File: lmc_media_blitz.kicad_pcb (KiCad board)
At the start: 2 copper layers, 76.2 x 114.3 mm, 83 parts, among them J3 Conn_ARM_JTAG_SWD_10, Q1 2N7002, Q2 2N7002, U1 TPS61222DCK, U10 SK9822, U11 SK9822, U12 SK9822, U13 SK9822, U14 SK9822, U2 XC6206PxxxMR, U4 ST25R3911B-AQFT, U5 LPC804M101JHI33, Y1 27.12MHz

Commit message: Updated MCU and connector pinout to make routing more convenient.  Power circuit still to be routed
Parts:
- added D1: SSL54B, Diode_SMD:D_SMB, F.Cu at (165.8, -34.2)
- added J4: Conn_01x12, Connector_PinSocket_2.54mm:PinSocket_1x12_P2.54mm_Vertical, F.Cu at (271.5, 88.6)
- added NT1: NetTie_2, NetTie:NetTie-2_SMD_Pad0.5mm, F.Cu at (163.9, -43.6)
- added R10: 10K, Resistor_SMD:R_0805_2012Metric, F.Cu at (259.9, 84.1)
- added R11: 10K, Resistor_SMD:R_0805_2012Metric, F.Cu at (269.5, 84.1)
- added R9: 10K, Resistor_SMD:R_0805_2012Metric, F.Cu at (250.3, 84.1)
- added SW1: SW_Push, Button_Switch_SMD:SW_Push_1P1T_XKB_TS-1187A, F.Cu at (246.6, 80.0)
- added SW2: SW_Push, Button_Switch_SMD:SW_Push_1P1T_XKB_TS-1187A, F.Cu at (256.3, 80.0)
- added SW3: SW_Push, Button_Switch_SMD:SW_Push_1P1T_XKB_TS-1187A, F.Cu at (266.0, 80.0)
- added TP10: TestPoint_Small, TestPoint:TestPoint_Pad_D1.5mm, F.Cu at (265.4, 86.9)
- added TP8: TestPoint_Small, TestPoint:TestPoint_Pad_D1.5mm, F.Cu at (253.7, 86.9)
- added TP9: TestPoint_Small, TestPoint:TestPoint_Pad_D1.5mm, F.Cu at (260.4, 86.9)
- added U3: STM32F030C8Tx, Package_QFP:LQFP-48_7x7mm_P0.5mm, F.Cu at (258.6, 103.6)
- added U6: SK9822, footprints:OPSCO_SK9822, F.Cu at (257.9, 126.2)
- added U7: SK9822, footprints:OPSCO_SK9822, F.Cu at (266.6, 126.2)
- added U8: SK9822, footprints:OPSCO_SK9822, F.Cu at (275.2, 126.2)
- C10, C14, C9: value 10nF -> 100nF
- C11: value 1uF -> 10nF
- C12, C16, C18, C6: value 10nF -> 1uF; footprint Capacitor_SMD:C_0603_1608Metric -> Capacitor_SMD:C_0805_2012Metric
- C13, C15: value 2.2uF -> 100nF
- C17: value 2.2uF -> 1uF; footprint Capacitor_SMD:C_0603_1608Metric -> Capacitor_SMD:C_0805_2012Metric
- C19: footprint Capacitor_SMD:C_0603_1608Metric -> Capacitor_SMD:C_0805_2012Metric
- C2: value 10uF -> 22uF
- C20: value 150pF -> 1uF
- C5: value 0.1uF -> 1uF; footprint Capacitor_SMD:C_0603_1608Metric -> Capacitor_SMD:C_0805_2012Metric
- C8: value 1uF -> 100nF
- J3: value Conn_ARM_JTAG_SWD_10 -> Conn_01x12; footprint Connector_PinHeader_1.27mm:PinHeader_2x05_P1.27mm_Vertical_SMD -> Connector_PinSocket_2.54mm:PinSocket_1x12_P2.54mm_Vertical
- L1: value 4.7uH -> 4u7; footprint Inductor_SMD:L_Taiyo-Yuden_MD-3030 -> Inductor_SMD:L_Changjiang_FNR4030S
- Q1, Q2: value 2N7002 -> BSS138W; footprint Package_TO_SOT_SMD:SOT-23 -> Package_TO_SOT_SMD:SOT-23W
- R1, R2: value 10K -> 4k7
- R7, R8: value 1R -> 10K
- TP4, TP5, TP6, TP7: footprint TestPoint:TestPoint_Pad_D2.0mm -> TestPoint:TestPoint_Pad_D1.5mm
- U1: value TPS61222DCK -> XC6206PxxxMR; footprint Package_TO_SOT_SMD:Texas_R-PDSO-G6 -> Package_TO_SOT_SMD:SOT-23-3
- U2: value XC6206PxxxMR -> TPS613222ADBV; footprint Package_TO_SOT_SMD:SOT-23-3 -> Package_TO_SOT_SMD:SOT-23-5
- U4: value ST25R3911B-AQFT -> SK9822; footprint Package_DFN_QFN:QFN-32-1EP_5x5mm_P0.5mm_EP3.6x3.6mm -> footprints:OPSCO_SK9822
- U5: value LPC804M101JHI33 -> SK9822; footprint Package_DFN_QFN:QFN-32-1EP_5x5mm_P0.5mm_EP3.7x3.7mm -> footprints:OPSCO_SK9822
- moved C15 132.4 mm to (270.6, 80.0), turned to 90 degrees
- moved C20 124.5 mm to (275.2, 130.3), turned to 180 degrees
- moved C1 123.4 mm to (164.9, -42.6), turned to 180 degrees
- moved C14 123.2 mm to (260.9, 80.0), turned to 90 degrees
- moved C2 123.0 mm to (168.7, -42.6), turned to 0 degrees
- moved U1 121.0 mm to (153.4, -44.1)
- moved R2 120.5 mm to (259.2, 93.7), turned to 180 degrees
- moved C3 119.1 mm to (150.6, -44.5)
- moved C4 119.0 mm to (156.2, -44.5), turned to 90 degrees
- moved R1 117.6 mm to (259.2, 91.7), turned to 180 degrees
- moved TP1 117.4 mm to (156.2, -38.3)
- moved TP2 117.4 mm to (188.8, -29.2)
- moved C10 116.6 mm to (261.9, 109.7), turned to 180 degrees
- moved U2 115.7 mm to (167.5, -39.1), turned to 90 degrees
- moved L1 115.3 mm to (163.1, -39.0), turned to -90 degrees
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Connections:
- C1 pad 2: +BATT -> /ADC_IN0
- C10 pad 1: +5V -> +3V3
- C11 pad 1: +5V -> +3V3
- C12 pad 1: /NFC/VSP_RF -> +3V3
- C13 pad 1: GND -> /SW1
- C13 pad 2: /NFC/VSP_RF -> GND
- C14 pad 1: /NFC/VSP_A -> /SW2
- C15 pad 1: GND -> /SW3
- C15 pad 2: /NFC/VSP_A -> GND
- C16 pad 1: /NFC/VSP_D -> +5V
- C17 pad 1: GND -> +5V
- C17 pad 2: /NFC/VSP_D -> GND
- C18 pad 1: /NFC/A_REF -> +5V
- C19 pad 1: /NFC/A_REF -> +5V
- C20 pad 1: GND -> +5V
- C20 pad 2: /NFC/RFI1 -> GND
- C6 pad 1: +3V3 -> +5V
- J3 pad 1: +3V3 -> +5V
- J3 pad 10: /nRESET -> GND
- J3 pad 2: /SWDIO -> GND
- J3 pad 3: GND -> +3V3
- J3 pad 4: /SWCLK -> +3V3
- J3 pad 6: unconnected-(J3-SWO/TDO-Pad6) -> /I2C1_SCL
- J3 pad 7: unconnected-(J3-KEY-Pad7) -> /I2C1_SDA
- J3 pad 8: unconnected-(J3-NC/TDI-Pad8) -> GND
- J3 pad 9: GND -> /BOOT0
- L1 pad 1: +BATT -> /ADC_IN0
- L1 pad 2: /L -> /BOOST_SW
- Q1 pad 1: /SPI0_MOSI -> /SPI1_SCK
- Q1 pad 2: /SPI0_MOSI -> /SPI1_SCK
- Q1 pad 3: /LEDs/SDI -> /LEDs/CKI
- Q2 pad 1: /SPI0_SCKB -> /SPI1_MOSI
- Q2 pad 2: /SPI0_SCKB -> /SPI1_MOSI
- Q2 pad 3: /LEDs/CKI -> /LEDs/SDI
- R1 pad 1: GND -> +3V3
- R1 pad 2: /SWCLK -> /I2C1_SDA
- R2 pad 2: /SWDIO -> /I2C1_SCL
- R3 pad 2: /SPI0_MOSI -> /nRST
- R4 pad 1: +5V -> +3V3
- R4 pad 2: /LEDs/SDI -> /SPI1_SCK
- R5 pad 1: +3V3 -> +5V
- R5 pad 2: /SPI0_SCKB -> /LEDs/CKI
- R6 pad 1: +5V -> +3V3
- R6 pad 2: /LEDs/CKI -> /SPI1_MOSI
- R7 pad 1: /NFC/ANT_MATCH1 -> +5V
- R7 pad 2: /NFC/ANT_DAMP1 -> /LEDs/SDI
- R8 pad 1: /NFC/ANT_MATCH2 -> /BOOT0
- R8 pad 2: /NFC/ANT_DAMP2 -> GND
- TP1 pad 1: GND -> +5V
- TP2 pad 1: /CAPT_X1 -> +3V3
- TP3 pad 1: +5V -> GND
- TP4 pad 1: +3V3 -> /ADC_IN0
- TP5 pad 1: +BATT -> /LEDs/CKI
- TP6 pad 1: /CAPT_X0 -> /SPI1_MISO
- TP7 pad 1: /CAPT_X2 -> /LEDs/SDI
- U1 pad 1: +BATT -> GND
- U1 pad 2: +5V -> +3V3
- U1 pad 3: GND -> +5V
- U2 pad 1: GND -> /BOOST_SW
- U2 pad 2: +3V3 -> GND
- U2 pad 3: +5V -> unconnected-(U2-NC-Pad3)
- U4 pad 1: +3V3 -> /LEDs/SDI
- U4 pad 2: unconnected-(U4-CSO-Pad2) -> /LEDs/CKI
- U4 pad 3: /NFC/VSP_D -> GND
- U4 pad 4: /NFC/XTO -> +5V
- U4 pad 5: /NFC/XTI -> /LEDs/LED2_CKI
- U4 pad 6: GND -> /LEDs/LED2_SDI
- U5 pad 1: /SPI0_SCKB -> /LEDs/LED2_SDI
- U5 pad 2: +BATT -> /LEDs/LED2_CKI
- U5 pad 3: unconnected-(U5-PIO0_12-Pad3) -> GND
- U5 pad 4: /nRESET -> +5V
- U5 pad 5: unconnected-(U5-PIO0_4/ADC_11/TRSTN-Pad5) -> /LEDs/LED3_CKI
- U5 pad 6: /SWCLK -> /LEDs/LED3_SDI
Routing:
- net (no net): track 0.00 -> 97.5 mm, vias 0 -> 2
- net GND: track 1.81 -> 74.3 mm, vias 169 -> 185
- net /nRST: track 0.00 -> 70.7 mm, vias 0 -> 4
- net +5V: track 225.4 -> 291.9 mm, vias 5 -> 6
- net /SPI0_MOSI: track 45.4 -> 0.00 mm, vias 4 -> 0
- net /SW1: track 0.00 -> 37.4 mm
- net +3V3: track 131.5 -> 167.4 mm, vias 3 -> 11
- net /SW3: track 0.00 -> 33.9 mm
- net /I2C1_SDA: track 0.00 -> 33.4 mm
- net /SW2: track 0.00 -> 29.5 mm
- net /I2C1_SCL: track 0.00 -> 27.6 mm
- net /SPI0_SCKB: track 25.1 -> 0.00 mm
- net /NFC_IRQ: track 19.8 -> 0.00 mm, vias 2 -> 0
- net /SPI2_NSS: track 0.00 -> 17.6 mm
- net /SPI2_SCK: track 0.00 -> 15.5 mm
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- added copper zone on F.Cu, net /BOOST_SW
- removed copper zone on F.Cu, net /L
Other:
- board text added: "NRST"
- board text added: "PA10/ RX"
- board text added: "PA9/TX"
- board text added: "PB12/CS"
- board text added: "PB13/SCK"
- board text added: "PB14/ MISO"
- board text added: "PB15/ MOSI"
- board text added: "SWCLK"
- board text added: "SWDIO"

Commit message: Changed board shape to be narrow around the pin headers to fit on a breadboard.  Still not sufficiently narrow
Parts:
- removed AE1: Antenna_Loop, footprints:badge_antenna
- removed C21, C36: 12pF, Capacitor_SMD:C_0805_2012Metric
- removed C22, C35: 100pF, Capacitor_SMD:C_0805_2012Metric
- removed C23, C24: 15pF, Capacitor_SMD:C_0603_1608Metric
- removed C25, C33: 470pF, Capacitor_SMD:C_0805_2012Metric
- removed C26, C34: 220pF, Capacitor_SMD:C_0805_2012Metric
- removed C27, C28, C29, C30, C31: 1uF, Capacitor_SMD:C_0805_2012Metric
- removed C32: 22nF, Capacitor_SMD:C_0805_2012Metric
- removed C37: 150pF, Capacitor_SMD:C_0805_2012Metric
- removed C38: 10uF, Capacitor_SMD:C_0805_2012Metric
- removed C39: 0.1uF, Capacitor_SMD:C_0603_1608Metric
- removed C40: 10nF, Capacitor_SMD:C_0603_1608Metric
- removed L2, L3: 270nH, Inductor_SMD:L_0805_2012Metric
- removed S1, S2, S3: ~, footprints:CapTouchButton
- removed U10, U11, U12, U13, U14: SK9822, footprints:OPSCO_SK9822
- removed Y1: 27.12MHz, Crystal:Crystal_SMD_Abracon_ABM8G-4Pin_3.2x2.5mm
- added TP11: TestPoint_Small, TestPoint:TestPoint_Pad_D1.5mm, F.Cu at (253.7, 86.9)
- TP1, TP2, TP3: footprint TestPoint:TestPoint_Pad_D2.0mm -> TestPoint:TestPoint_Pad_D1.5mm
- moved NT1 107.4 mm to (138.7, 60.7), turned to 90 degrees
- moved C1 101.9 mm to (138.7, 55.8), turned to -90 degrees
- moved C2 98.6 mm to (138.7, 51.3), turned to 90 degrees
- moved C3 98.2 mm to (154.2, 53.7)
- moved C4 98.2 mm to (159.8, 53.7)
- moved U1 98.2 mm to (157.0, 54.0)
- moved L1 97.2 mm to (142.2, 55.9), turned to 0 degrees
- moved U2 94.2 mm to (142.0, 51.6), turned to 180 degrees
- moved TP2 91.3 mm to (159.8, 57.4)
- moved TP1 90.0 mm to (151.6, 51.6)
- moved D1 89.6 mm to (147.3, 53.5), turned to -90 degrees
- moved TP8 35.6 mm to (252.5, 122.4)
- moved Q2 33.7 mm to (257.0, 118.4)
- moved R6 33.7 mm to (257.0, 115.3)
- moved R7 33.7 mm to (257.0, 121.4)
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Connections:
- C5 pad 1: +3V3 -> +5V
- C6 pad 1: +5V -> +3V3
- J3 pad 1: +5V -> GND
- J3 pad 11: /PB2 -> /GPIO_EXTI2
- J3 pad 12: /GPIO_EXTI10 -> /PA1
- J3 pad 2: GND -> +3V3
- J3 pad 4: +3V3 -> +5V
- TP10 pad 1: /SW3 -> /SW2
- TP5 pad 1: /LEDs/CKI -> /SPI1_NSS
- TP6 pad 1: /SPI1_MISO -> /LEDs/CKI
- TP7 pad 1: /LEDs/SDI -> /SPI1_MISO
- TP8 pad 1: /SW1 -> /LEDs/SDI
- TP9 pad 1: /SW2 -> /SW1
- U3 pad 11: unconnected-(U3-PA1-Pad11) -> /PA1
- U3 pad 12: unconnected-(U3-PA2-Pad12) -> /GPIO_EXTI2
- U3 pad 14: unconnected-(U3-PA4-Pad14) -> /SPI1_NSS
- U3 pad 21: /GPIO_EXTI10 -> unconnected-(U3-PB10-Pad21)
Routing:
- net +5V: track 291.9 -> 72.1 mm, vias 6 -> 4
- net +3V3: track 167.4 -> 45.8 mm, vias 11 -> 10
- net (no net): track 97.5 -> 0.00 mm, vias 2 -> 0
- net /CAPT_YH: track 79.5 -> 0.00 mm, vias 4 -> 0
- net +BATT: track 85.4 -> 7.62 mm, vias 2 -> 0
- net /CAPT_X2: track 51.6 -> 0.00 mm, vias 1 -> 0
- net /nRST: track 70.7 -> 25.0 mm, vias 4 -> 0
- net /CAPT_X1: track 43.7 -> 0.00 mm, vias 1 -> 0
- net /NFC/RFI2: track 34.6 -> 0.00 mm, vias 2 -> 0
- net /CAPT_X0: track 33.6 -> 0.00 mm, vias 1 -> 0
- net /NFC/RFI1: track 33.2 -> 0.00 mm, vias 2 -> 0
- net /CAPT_YL: track 32.4 -> 0.00 mm
- net /PA1: track 0.00 -> 21.1 mm
- net /BOOT0: track 11.1 -> 32.2 mm
- net /LEDs/LED3_CKI: track 22.6 -> 3.44 mm, vias 2 -> 0
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- added copper zone on F.Cu, net /ADC_IN0
- removed copper zone on F.Cu, net +BATT
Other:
- board text added: "+BATT"
- board text added: "BOOT0"
- board text added: "PA1"
- board text added: "PA2/ IRQ"
- board text added: "PA4"
- board text added: "PA6"
- board text added: "PB6/ SCL"
- board text added: "PB7 SDA"
- board text added: "STM32F0-PROTO V0.1"
- board text removed: "BAT+"

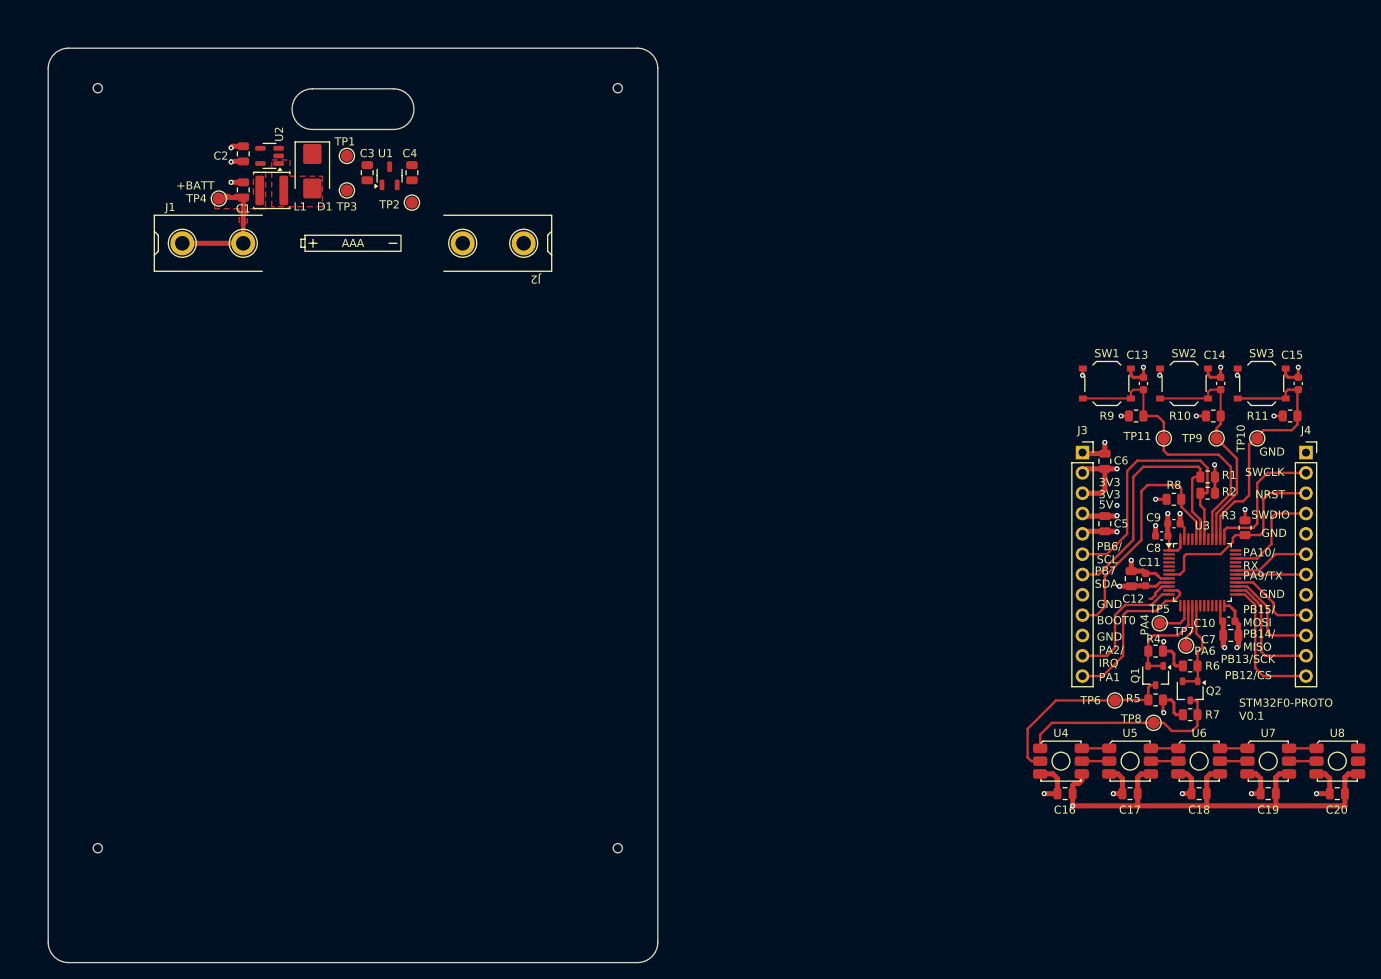
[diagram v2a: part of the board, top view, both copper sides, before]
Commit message: Changed 1x12 connectors to 2x12 connectors, and made board shape rectangular
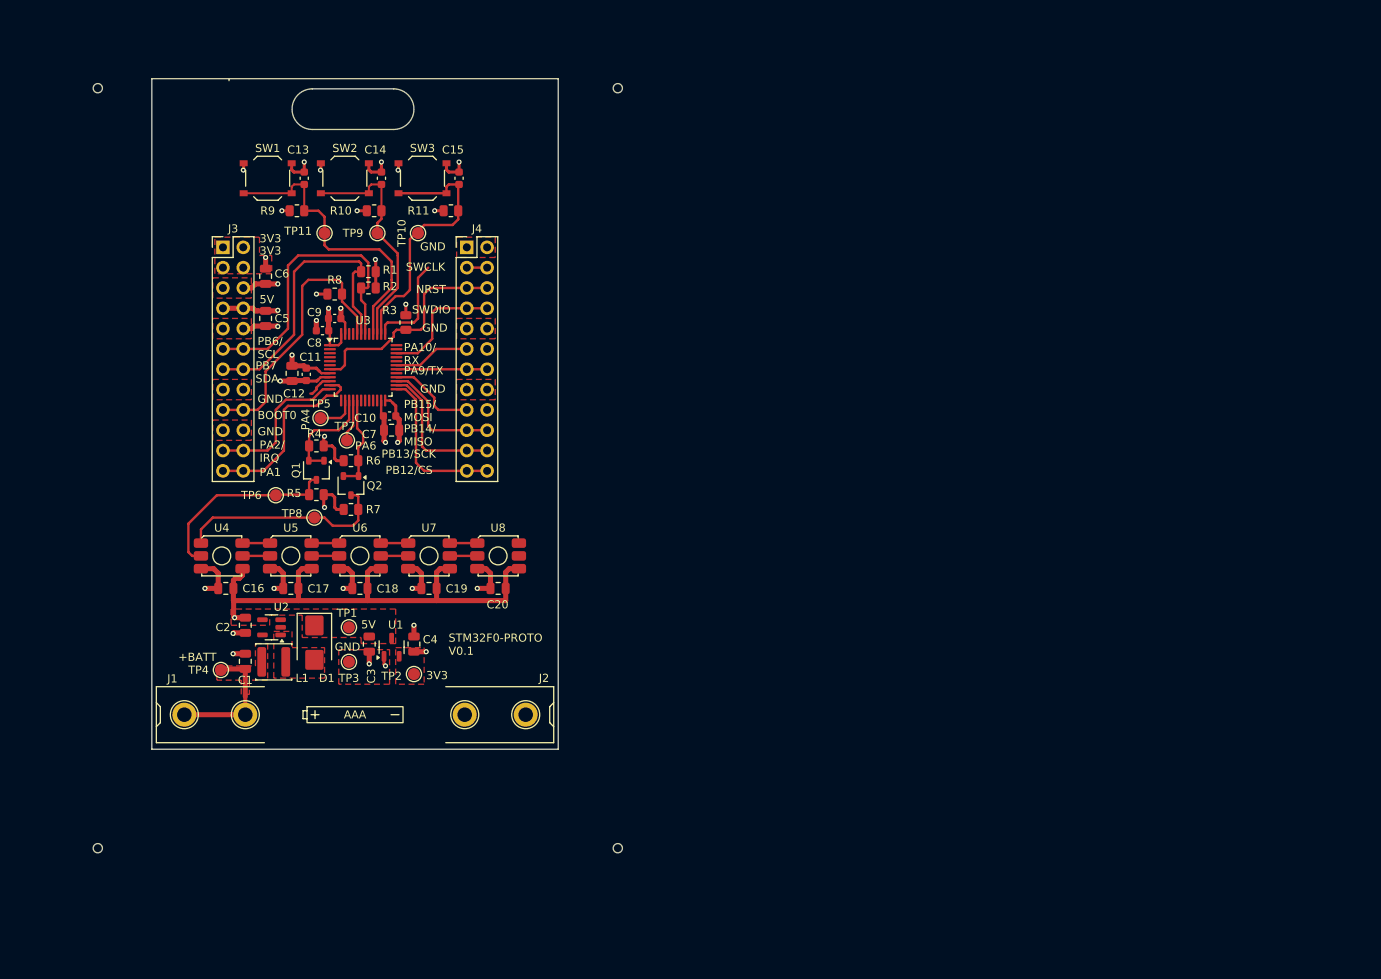
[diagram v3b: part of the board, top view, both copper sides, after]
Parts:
- J3, J4: value Conn_01x12 -> Conn_02x12_Odd_Even; footprint Connector_PinSocket_2.54mm:PinSocket_1x12_P2.54mm_Vertical -> Connector_PinHeader_2.54mm:PinHeader_2x12_P2.54mm_Vertical
- moved J3 110.5 mm to (136.1, 63.0)
- moved C10 108.0 mm to (157.0, 84.1)
- moved C11 108.0 mm to (146.6, 78.9)
- moved C14 108.0 mm to (156.0, 54.4)
- moved C17 108.0 mm to (144.6, 105.6)
- moved C18 108.0 mm to (153.3, 105.6)
- moved J4 108.0 mm to (166.6, 63.0)
- moved Q2 108.0 mm to (152.1, 92.8)
- moved R1 108.0 mm to (154.3, 66.0)
- moved R2 108.0 mm to (154.3, 68.1)
- moved R3 108.0 mm to (159.0, 72.4)
- moved R6 108.0 mm to (152.1, 89.7)
- moved R7 108.0 mm to (152.1, 95.8)
- moved SW2 108.0 mm to (151.4, 54.4)
- moved TP10 108.0 mm to (160.5, 61.2)
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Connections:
- J3 pad 1: GND -> +3V3
- J3 pad 11: /GPIO_EXTI2 -> /I2C1_SCL
- J3 pad 12: /PA1 -> /I2C1_SCL
- J3 pad 4: +5V -> +3V3
- J3 pad 6: /I2C1_SCL -> GND
- J3 pad 7: /I2C1_SDA -> +5V
- J3 pad 8: GND -> +5V
- J3 pad 9: /BOOT0 -> GND
- J4 pad 10: /SPI2_MISO -> GND
- J4 pad 11: /SPI2_SCK -> /USART1_RX
- J4 pad 12: /SPI2_NSS -> /USART1_RX
- J4 pad 2: /SWCLK -> GND
- J4 pad 3: /nRST -> /SWCLK
- J4 pad 4: /SWDIO -> /SWCLK
- J4 pad 5: GND -> /nRST
- J4 pad 6: /USART1_RX -> /nRST
- J4 pad 7: /USART1_TX -> /SWDIO
- J4 pad 8: GND -> /SWDIO
- J4 pad 9: /SPI2_MOSI -> GND
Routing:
- net +3V3: track 45.8 -> 38.8 mm, vias 10 -> 11
- net GND: track 69.9 -> 74.8 mm, vias 21 -> 23
- net +5V: track 72.1 -> 77.0 mm, vias 4 -> 3
- net /PA1: track 21.1 -> 23.7 mm
- net /I2C1_SDA: track 35.1 -> 37.6 mm
- net /USART1_TX: track 8.79 -> 11.3 mm
- net /SPI2_MISO: track 13.1 -> 15.7 mm
- net /I2C1_SCL: track 35.4 -> 37.9 mm
- net /SPI2_NSS: track 17.6 -> 20.2 mm
- net /SWDIO: track 13.1 -> 15.6 mm
- net /SPI2_SCK: track 15.5 -> 18.1 mm
- net /GPIO_EXTI2: track 16.4 -> 18.9 mm
- net /BOOT0: track 32.2 -> 34.7 mm
- net /nRST: track 25.0 -> 27.6 mm
- net /SWCLK: track 17.3 -> 15.0 mm
- added copper zone on F.Cu, net +3V3
- added copper zone on F.Cu, net +5V
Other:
- board size 76.2 x 114.3 mm -> 50.8 x 83.8 mm
